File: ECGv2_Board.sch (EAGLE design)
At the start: 37 parts, among them IC1 LF347D, IC2 LF347D, IC3 TINY15LS, Q1 BS250

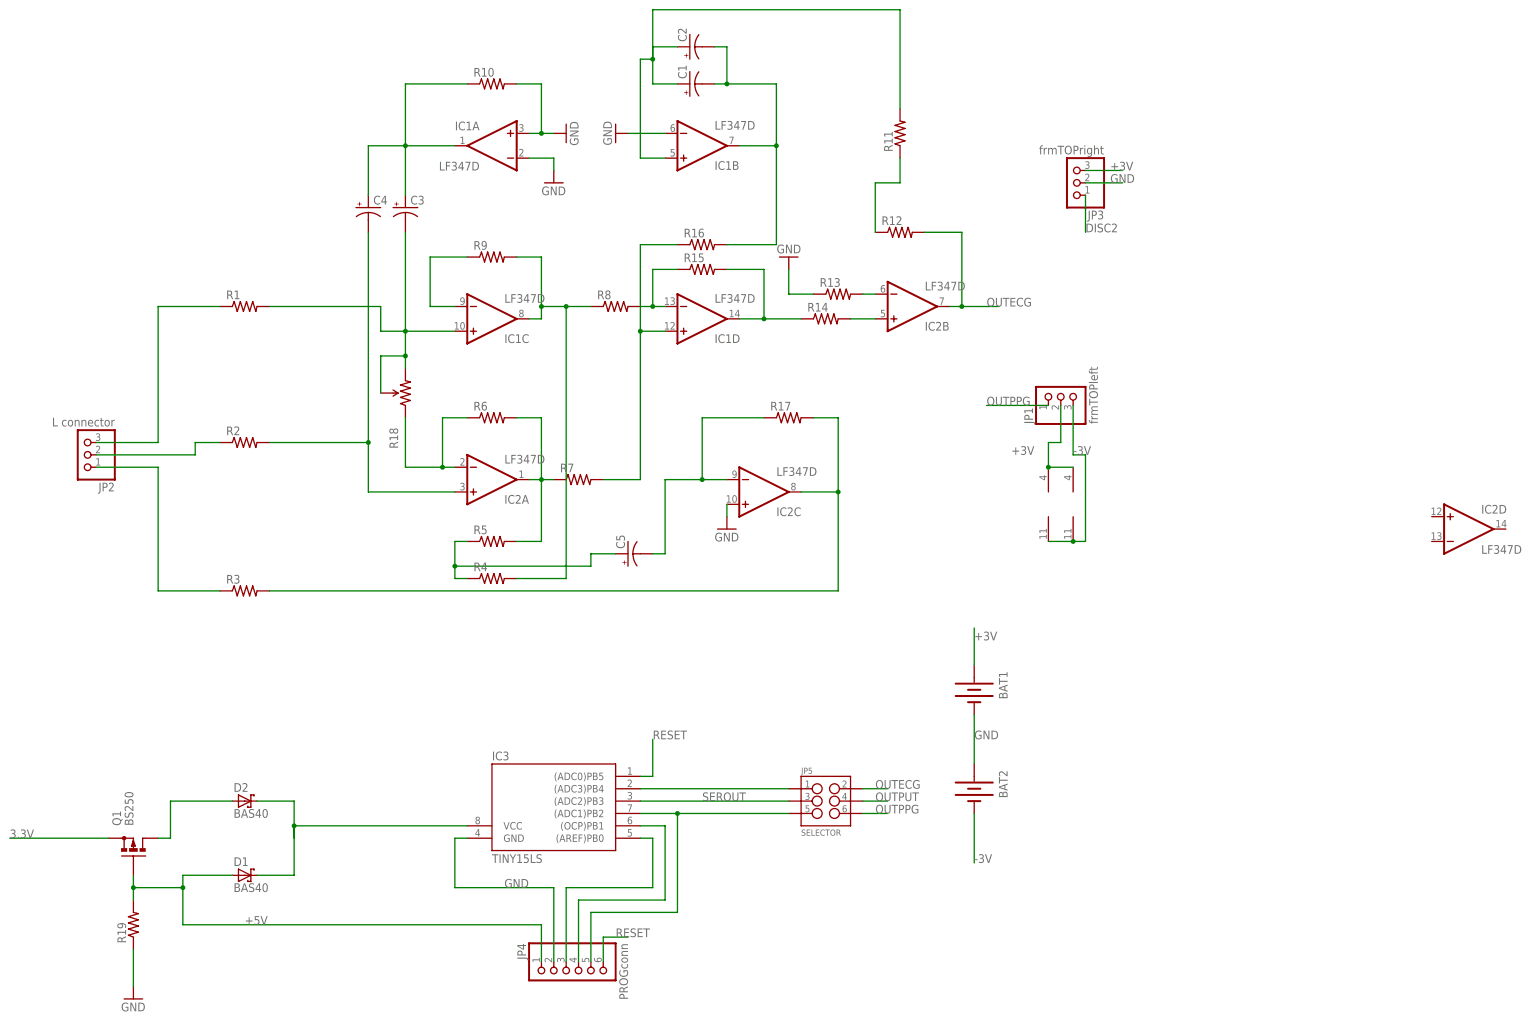
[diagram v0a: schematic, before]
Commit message: -added missing connection
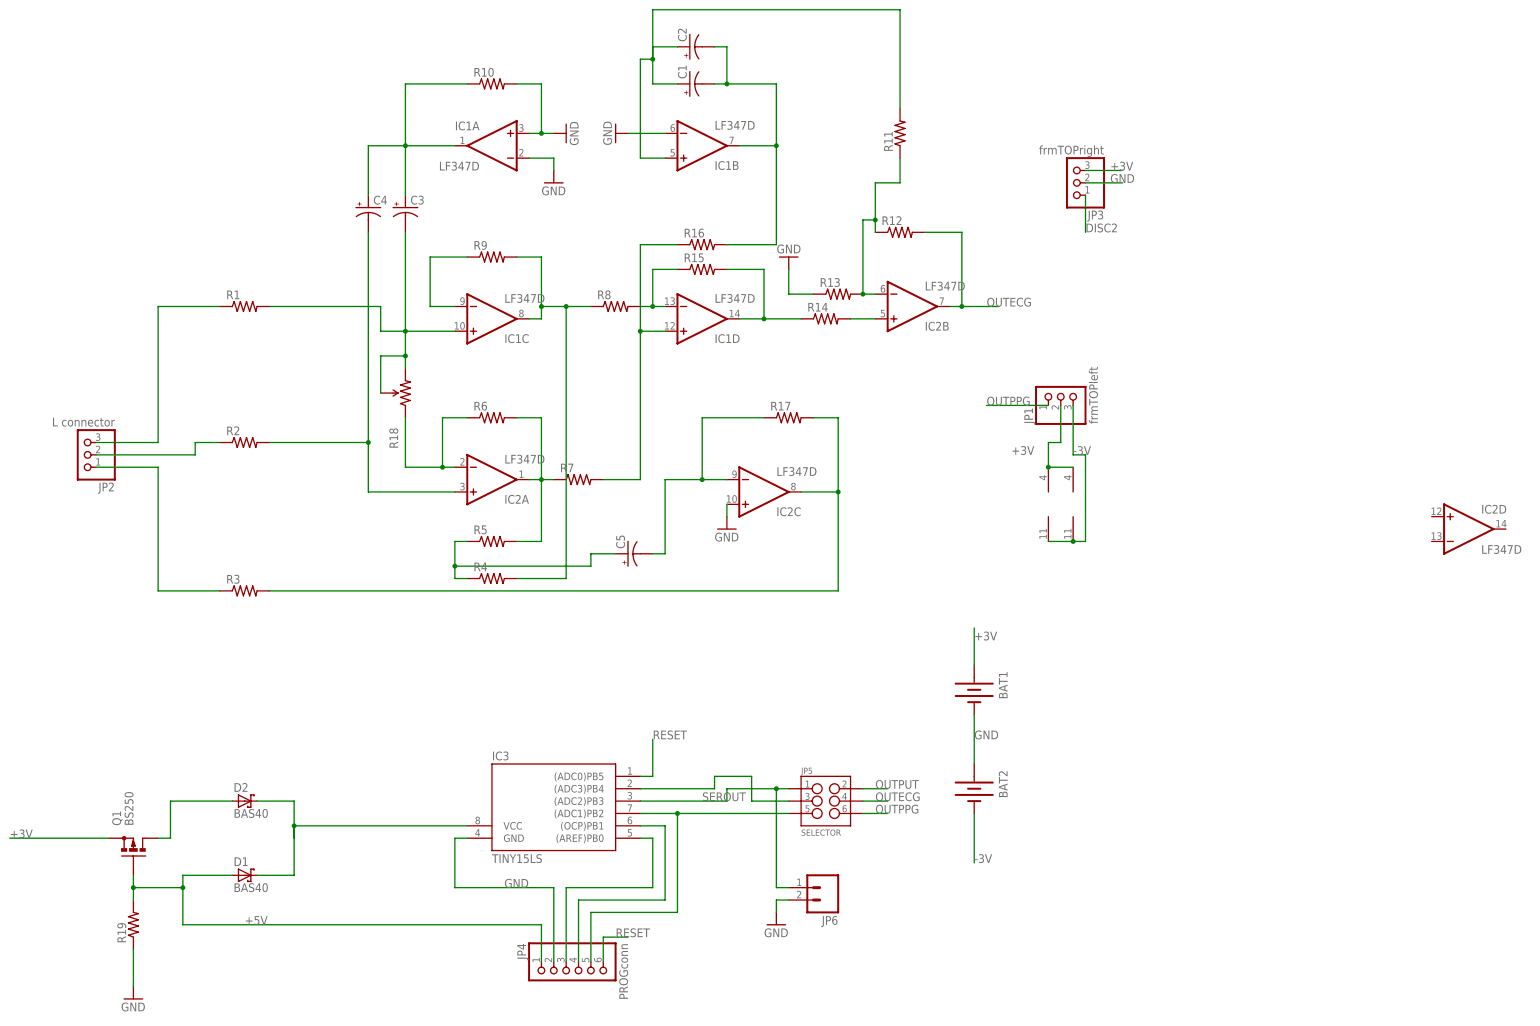
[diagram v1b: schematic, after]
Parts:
- added JP6: (no value), SparkFun-Connectors:M02PTH
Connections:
- removed net 3.3V: Q1.S
- removed net N$27: IC3.(ADC3)PB4, JP5.1
- removed net N$3: R11.1, R12.1
- new net N$28: IC3.(ADC3)PB4, JP5.3
- net +3V: now also Q1.S
- net GND: now also JP6.2
- net N$5: now also R11.1, R12.1
- net OUTECG: now also JP5.4; no longer JP5.2
- net OUTPUT: now also JP5.2; no longer JP5.4
- net SEROUT: now also JP5.1, JP6.1; no longer JP5.3
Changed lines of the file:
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@@
 <part name="GND6" library="supply1" deviceset="GND" device=""/>
 <part name="JP5" library="SparkFun-Connectors" deviceset="M03X2" device="FEMALE" value="SELECTOR"/>
+<part name="JP6" library="SparkFun-Connectors" deviceset="M02" device="PTH"/>
+<part name="GND7" library="supply1" deviceset="GND" device=""/>
 </parts>
 <sheets>
@@
 <instance part="GND6" gate="1" x="-58.42" y="-104.14"/>
 <instance part="JP5" gate="G$1" x="83.82" y="-63.5"/>
+<instance part="JP6" gate="G$1" x="83.82" y="-81.28" rot="R180"/>
+<instance part="GND7" gate="1" x="73.66" y="-88.9"/>
 </instances>
 <busses>
@@
 <wire x1="-58.42" y1="-101.6" x2="-58.42" y2="-93.98" width="0.1524" layer="91"/>
 </segment>
-</net>
-<net name="N$3" class="0">
-<segment>
-<pinref part="R11" gate="G$1" pin="1"/>
-<wire x1="99.06" y1="68.58" x2="99.06" y2="63.5" width="0.1524" layer="91"/>
-<pinref part="R12" gate="G$1" pin="1"/>
-<wire x1="99.06" y1="63.5" x2="93.98" y2="63.5" width="0.1524" layer="91"/>
-<wire x1="93.98" y1="63.5" x2="93.98" y2="53.34" width="0.1524" layer="91"/>
+<segment>
+<pinref part="JP6" gate="G$1" pin="2"/>
+<pinref part="GND7" gate="1" pin="GND"/>
+<wire x1="76.2" y1="-83.82" x2="73.66" y2="-83.82" width="0.1524" layer="91"/>
+<wire x1="73.66" y1="-83.82" x2="73.66" y2="-86.36" width="0.1524" layer="91"/>
 </segment>
 </net>
@@
 </segment>
 <segment>
-<pinref part="JP5" gate="G$1" pin="2"/>
-<wire x1="91.44" y1="-60.96" x2="96.52" y2="-60.96" width="0.1524" layer="91"/>
-<label x="93.98" y="-60.96" size="1.778" layer="95"/>
+<pinref part="JP5" gate="G$1" pin="4"/>
+<wire x1="91.44" y1="-63.5" x2="96.52" y2="-63.5" width="0.1524" layer="91"/>
+<label x="93.98" y="-63.5" size="1.778" layer="95"/>
 </segment>
 </net>
@@
 <pinref part="IC2" gate="B" pin="-IN"/>
 <wire x1="91.44" y1="40.64" x2="93.98" y2="40.64" width="0.1524" layer="91"/>
+<wire x1="91.44" y1="40.64" x2="91.44" y2="55.88" width="0.1524" layer="91"/>
+<junction x="91.44" y="40.64"/>
+<pinref part="R11" gate="G$1" pin="1"/>
+<wire x1="99.06" y1="68.58" x2="99.06" y2="63.5" width="0.1524" layer="91"/>
+<pinref part="R12" gate="G$1" pin="1"/>
+<wire x1="99.06" y1="63.5" x2="93.98" y2="63.5" width="0.1524" layer="91"/>
+<wire x1="93.98" y1="63.5" x2="93.98" y2="55.88" width="0.1524" layer="91"/>
+<wire x1="93.98" y1="55.88" x2="93.98" y2="53.34" width="0.1524" layer="91"/>
+<wire x1="91.44" y1="55.88" x2="93.98" y2="55.88" width="0.1524" layer="91"/>
+<junction x="93.98" y="55.88"/>
 </segment>
 </net>
@@
 <wire x1="114.3" y1="-35.56" x2="114.3" y2="-27.94" width="0.1524" layer="91"/>
 <label x="114.3" y="-30.48" size="1.778" layer="95"/>
+</segment>
+<segment>
+<pinref part="Q1" gate="1" pin="S"/>
+<wire x1="-63.5" y1="-71.12" x2="-83.82" y2="-71.12" width="0.1524" layer="91"/>
+<label x="-83.82" y="-71.12" size="1.778" layer="95"/>
 </segment>
 </net>
@@
 <net name="SEROUT" class="0">
 <segment>
+<label x="58.42" y="-63.5" size="1.778" layer="95"/>
+<pinref part="JP6" gate="G$1" pin="1"/>
+<wire x1="73.66" y1="-81.28" x2="76.2" y2="-81.28" width="0.1524" layer="91"/>
 <pinref part="IC3" gate="G$1" pin="(ADC2)PB3"/>
-<label x="58.42" y="-63.5" size="1.778" layer="95"/>
-<pinref part="JP5" gate="G$1" pin="3"/>
-<wire x1="45.72" y1="-63.5" x2="76.2" y2="-63.5" width="0.1524" layer="91"/>
+<wire x1="45.72" y1="-63.5" x2="63.5" y2="-63.5" width="0.1524" layer="91"/>
+<wire x1="63.5" y1="-63.5" x2="63.5" y2="-60.96" width="0.1524" layer="91"/>
+<pinref part="JP5" gate="G$1" pin="1"/>
+<wire x1="63.5" y1="-60.96" x2="73.66" y2="-60.96" width="0.1524" layer="91"/>
+<wire x1="73.66" y1="-60.96" x2="76.2" y2="-60.96" width="0.1524" layer="91"/>
+<wire x1="73.66" y1="-81.28" x2="73.66" y2="-60.96" width="0.1524" layer="91"/>
+<junction x="73.66" y="-60.96"/>
 </segment>
 </net>
@@
 </segment>
 </net>
-<net name="3.3V" class="0">
-<segment>
-<pinref part="Q1" gate="1" pin="S"/>
-<wire x1="-63.5" y1="-71.12" x2="-83.82" y2="-71.12" width="0.1524" layer="91"/>
-<label x="-83.82" y="-71.12" size="1.778" layer="95"/>
-</segment>
-</net>
 <net name="N$25" class="0">
 <segment>
@@
 </segment>
 </net>
+<net name="N$28" class="0">
+<segment>
+<pinref part="IC3" gate="G$1" pin="(ADC3)PB4"/>
+<wire x1="45.72" y1="-60.96" x2="60.96" y2="-60.96" width="0.1524" layer="91"/>
+<wire x1="60.96" y1="-60.96" x2="60.96" y2="-58.42" width="0.1524" layer="91"/>
+<wire x1="60.96" y1="-58.42" x2="68.58" y2="-58.42" width="0.1524" layer="91"/>
+<wire x1="68.58" y1="-58.42" x2="68.58" y2="-63.5" width="0.1524" layer="91"/>
+<pinref part="JP5" gate="G$1" pin="3"/>
+<wire x1="68.58" y1="-63.5" x2="76.2" y2="-63.5" width="0.1524" layer="91"/>
+</segment>
+</net>
 <net name="OUTPUT" class="0">
 <segment>
-<pinref part="JP5" gate="G$1" pin="4"/>
-<wire x1="91.44" y1="-63.5" x2="96.52" y2="-63.5" width="0.1524" layer="91"/>
-<label x="93.98" y="-63.5" size="1.778" layer="95"/>
-</segment>
-</net>
-<net name="N$27" class="0">
-<segment>
-<pinref part="IC3" gate="G$1" pin="(ADC3)PB4"/>
-<pinref part="JP5" gate="G$1" pin="1"/>
-<wire x1="45.72" y1="-60.96" x2="76.2" y2="-60.96" width="0.1524" layer="91"/>
-</segment>
-</net>
+<pinref part="JP5" gate="G$1" pin="2"/>
+<wire x1="91.44" y1="-60.96" x2="96.52" y2="-60.96" width="0.1524" layer="91"/>
+<label x="93.98" y="-60.96" size="1.778" layer="95"/>
+</segment>
+</net>

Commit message: Major changes
-final commit
-some corrections
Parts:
- Q1: value BS250 -> BSS84; device transistor-small-signal:BS250 -> transistor-small-signal:BSS84
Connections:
- removed net N$11: IC1C.-IN, R9.1
- new net N$3: IC1C.-IN, R18.CW, R18.WIPER, R9.1
- net GND: now also IC1B.+IN; no longer IC1B.-IN
- net N$19: no longer R18.CW, R18.WIPER
- net N$2: now also IC1B.-IN; no longer IC1B.+IN
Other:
- moved on the sheet: R7, R8
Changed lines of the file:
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@@
 <part name="BAT1" library="SparkFun-Electromechanical" deviceset="BATTERY" device="245MM"/>
 <part name="BAT2" library="SparkFun-Electromechanical" deviceset="BATTERY" device="245MM"/>
-<part name="Q1" library="transistor-small-signal" deviceset="BS250" device=""/>
+<part name="Q1" library="transistor-small-signal" deviceset="BSS84" device=""/>
 <part name="R19" library="SparkFun-Passives" deviceset="RESISTOR" device="0402-RES"/>
 <part name="GND6" library="supply1" deviceset="GND" device=""/>
@@
 <instance part="GND1" gate="1" x="27.94" y="63.5"/>
 <instance part="GND2" gate="1" x="30.48" y="73.66" rot="R90"/>
-<instance part="GND3" gate="1" x="40.64" y="73.66" rot="R270"/>
+<instance part="GND3" gate="1" x="40.64" y="68.58" rot="R270"/>
 <instance part="GND4" gate="1" x="63.5" y="-7.62"/>
 <instance part="GND5" gate="1" x="76.2" y="48.26" rot="R180"/>
@@
 <instance part="R5" gate="G$1" x="15.24" y="-10.16"/>
 <instance part="R6" gate="G$1" x="15.24" y="15.24"/>
-<instance part="R7" gate="G$1" x="33.02" y="2.54"/>
-<instance part="R8" gate="G$1" x="40.64" y="38.1"/>
+<instance part="R7" gate="G$1" x="38.1" y="2.54"/>
+<instance part="R8" gate="G$1" x="38.1" y="38.1"/>
 <instance part="R9" gate="G$1" x="15.24" y="48.26"/>
 <instance part="R10" gate="G$1" x="15.24" y="83.82"/>
@@
 <instance part="BAT1" gate="G$1" x="114.3" y="-40.64" rot="R270"/>
 <instance part="BAT2" gate="G$1" x="114.3" y="-60.96" rot="R270"/>
-<instance part="Q1" gate="1" x="-58.42" y="-73.66" rot="R90"/>
+<instance part="Q1" gate="G$1" x="-60.96" y="-71.12" rot="R90"/>
 <instance part="R19" gate="G$1" x="-58.42" y="-88.9" rot="R90"/>
 <instance part="GND6" gate="1" x="-58.42" y="-104.14"/>
@@
 <wire x1="48.26" y1="91.44" x2="53.34" y2="91.44" width="0.1524" layer="91"/>
 <wire x1="48.26" y1="88.9" x2="45.72" y2="88.9" width="0.1524" layer="91"/>
-<wire x1="45.72" y1="88.9" x2="45.72" y2="68.58" width="0.1524" layer="91"/>
 <junction x="48.26" y="88.9"/>
 <wire x1="48.26" y1="88.9" x2="48.26" y2="99.06" width="0.1524" layer="91"/>
@@
 <wire x1="48.26" y1="99.06" x2="99.06" y2="99.06" width="0.1524" layer="91"/>
 <wire x1="99.06" y1="99.06" x2="99.06" y2="78.74" width="0.1524" layer="91"/>
-<pinref part="IC1" gate="B" pin="+IN"/>
-<wire x1="45.72" y1="68.58" x2="50.8" y2="68.58" width="0.1524" layer="91"/>
+<wire x1="45.72" y1="88.9" x2="45.72" y2="73.66" width="0.1524" layer="91"/>
+<pinref part="IC1" gate="B" pin="-IN"/>
+<wire x1="45.72" y1="73.66" x2="50.8" y2="73.66" width="0.1524" layer="91"/>
 </segment>
 </net>
@@
 </segment>
 <segment>
-<pinref part="GND3" gate="1" pin="GND"/>
-<pinref part="IC1" gate="B" pin="-IN"/>
-<wire x1="43.18" y1="73.66" x2="50.8" y2="73.66" width="0.1524" layer="91"/>
-</segment>
-<segment>
 <pinref part="GND4" gate="1" pin="GND"/>
 <pinref part="IC2" gate="C" pin="+IN"/>
@@
 <wire x1="76.2" y1="-83.82" x2="73.66" y2="-83.82" width="0.1524" layer="91"/>
 <wire x1="73.66" y1="-83.82" x2="73.66" y2="-86.36" width="0.1524" layer="91"/>
+</segment>
+<segment>
+<pinref part="GND3" gate="1" pin="GND"/>
+<pinref part="IC1" gate="B" pin="+IN"/>
+<wire x1="43.18" y1="68.58" x2="50.8" y2="68.58" width="0.1524" layer="91"/>
 </segment>
 </net>
@@
 <wire x1="48.26" y1="45.72" x2="48.26" y2="38.1" width="0.1524" layer="91"/>
 <pinref part="R8" gate="G$1" pin="2"/>
-<wire x1="48.26" y1="38.1" x2="45.72" y2="38.1" width="0.1524" layer="91"/>
+<wire x1="48.26" y1="38.1" x2="43.18" y2="38.1" width="0.1524" layer="91"/>
 <pinref part="IC1" gate="D" pin="-IN"/>
 <wire x1="50.8" y1="38.1" x2="48.26" y2="38.1" width="0.1524" layer="91"/>
@@
 <wire x1="53.34" y1="50.8" x2="45.72" y2="50.8" width="0.1524" layer="91"/>
 <pinref part="R7" gate="G$1" pin="2"/>
-<wire x1="38.1" y1="2.54" x2="45.72" y2="2.54" width="0.1524" layer="91"/>
+<wire x1="43.18" y1="2.54" x2="45.72" y2="2.54" width="0.1524" layer="91"/>
 <wire x1="45.72" y1="2.54" x2="45.72" y2="33.02" width="0.1524" layer="91"/>
 <pinref part="IC1" gate="D" pin="+IN"/>
@@
 <wire x1="22.86" y1="2.54" x2="25.4" y2="2.54" width="0.1524" layer="91"/>
 <pinref part="R6" gate="G$1" pin="2"/>
-<wire x1="25.4" y1="2.54" x2="27.94" y2="2.54" width="0.1524" layer="91"/>
+<wire x1="25.4" y1="2.54" x2="33.02" y2="2.54" width="0.1524" layer="91"/>
 <wire x1="20.32" y1="15.24" x2="25.4" y2="15.24" width="0.1524" layer="91"/>
 <wire x1="25.4" y1="15.24" x2="25.4" y2="2.54" width="0.1524" layer="91"/>
@@
 <segment>
 <pinref part="R8" gate="G$1" pin="1"/>
-<wire x1="35.56" y1="38.1" x2="30.48" y2="38.1" width="0.1524" layer="91"/>
+<wire x1="33.02" y1="38.1" x2="30.48" y2="38.1" width="0.1524" layer="91"/>
 <wire x1="30.48" y1="38.1" x2="25.4" y2="38.1" width="0.1524" layer="91"/>
 <wire x1="25.4" y1="38.1" x2="25.4" y2="35.56" width="0.1524" layer="91"/>
@@
 </segment>
 </net>
-<net name="N$11" class="0">
-<segment>
-<pinref part="R9" gate="G$1" pin="1"/>
-<wire x1="10.16" y1="48.26" x2="2.54" y2="48.26" width="0.1524" layer="91"/>
-<wire x1="2.54" y1="48.26" x2="2.54" y2="38.1" width="0.1524" layer="91"/>
-<pinref part="IC1" gate="C" pin="-IN"/>
-<wire x1="2.54" y1="38.1" x2="7.62" y2="38.1" width="0.1524" layer="91"/>
-</segment>
-</net>
 <net name="N$12" class="0">
 <segment>
@@
 <net name="N$19" class="0">
 <segment>
-<pinref part="R18" gate="R?" pin="WIPER"/>
-<wire x1="-7.62" y1="20.32" x2="-7.62" y2="27.94" width="0.1524" layer="91"/>
-<pinref part="R18" gate="R?" pin="CW"/>
-<wire x1="-7.62" y1="27.94" x2="-2.54" y2="27.94" width="0.1524" layer="91"/>
-<wire x1="-2.54" y1="27.94" x2="-2.54" y2="25.4" width="0.1524" layer="91"/>
-<pinref part="C3" gate="G$1" pin="-"/>
-<wire x1="-2.54" y1="53.34" x2="-2.54" y2="33.02" width="0.1524" layer="91"/>
 <pinref part="R1" gate="G$1" pin="2"/>
 <wire x1="-30.48" y1="38.1" x2="-7.62" y2="38.1" width="0.1524" layer="91"/>
 <wire x1="-7.62" y1="38.1" x2="-7.62" y2="33.02" width="0.1524" layer="91"/>
+<pinref part="IC1" gate="C" pin="+IN"/>
 <wire x1="-7.62" y1="33.02" x2="-2.54" y2="33.02" width="0.1524" layer="91"/>
+<pinref part="C3" gate="G$1" pin="-"/>
+<wire x1="-2.54" y1="33.02" x2="7.62" y2="33.02" width="0.1524" layer="91"/>
+<wire x1="-2.54" y1="53.34" x2="-2.54" y2="33.02" width="0.1524" layer="91"/>
 <junction x="-2.54" y="33.02"/>
-<wire x1="-2.54" y1="27.94" x2="-2.54" y2="33.02" width="0.1524" layer="91"/>
-<junction x="-2.54" y="27.94"/>
-<pinref part="IC1" gate="C" pin="+IN"/>
-<wire x1="-2.54" y1="33.02" x2="7.62" y2="33.02" width="0.1524" layer="91"/>
 </segment>
 </net>
@@
 </segment>
 <segment>
-<pinref part="Q1" gate="1" pin="S"/>
-<wire x1="-63.5" y1="-71.12" x2="-83.82" y2="-71.12" width="0.1524" layer="91"/>
+<pinref part="Q1" gate="G$1" pin="S"/>
+<wire x1="-66.04" y1="-71.12" x2="-83.82" y2="-71.12" width="0.1524" layer="91"/>
 <label x="-83.82" y="-71.12" size="1.778" layer="95"/>
 </segment>
@@
 <wire x1="-48.26" y1="-88.9" x2="-48.26" y2="-81.28" width="0.1524" layer="91"/>
 <pinref part="R19" gate="G$1" pin="2"/>
-<pinref part="Q1" gate="1" pin="G"/>
+<pinref part="Q1" gate="G$1" pin="G"/>
 <wire x1="-58.42" y1="-83.82" x2="-58.42" y2="-81.28" width="0.1524" layer="91"/>
-<wire x1="-58.42" y1="-81.28" x2="-58.42" y2="-78.74" width="0.1524" layer="91"/>
+<wire x1="-58.42" y1="-81.28" x2="-63.5" y2="-76.2" width="0.1524" layer="91"/>
 <wire x1="-48.26" y1="-81.28" x2="-58.42" y2="-81.28" width="0.1524" layer="91"/>
 <junction x="-58.42" y="-81.28"/>
@@
 <wire x1="-38.1" y1="-63.5" x2="-50.8" y2="-63.5" width="0.1524" layer="91"/>
 <wire x1="-50.8" y1="-63.5" x2="-50.8" y2="-71.12" width="0.1524" layer="91"/>
-<pinref part="Q1" gate="1" pin="D"/>
-<wire x1="-50.8" y1="-71.12" x2="-53.34" y2="-71.12" width="0.1524" layer="91"/>
+<pinref part="Q1" gate="G$1" pin="D"/>
+<wire x1="-50.8" y1="-71.12" x2="-55.88" y2="-71.12" width="0.1524" layer="91"/>
 </segment>
 </net>
@@
 </segment>
 </net>
+<net name="N$3" class="0">
+<segment>
+<pinref part="R18" gate="R?" pin="CW"/>
+<wire x1="-2.54" y1="27.94" x2="-2.54" y2="25.4" width="0.1524" layer="91"/>
+<wire x1="-7.62" y1="27.94" x2="-2.54" y2="27.94" width="0.1524" layer="91"/>
+<pinref part="R18" gate="R?" pin="WIPER"/>
+<wire x1="-7.62" y1="20.32" x2="-7.62" y2="27.94" width="0.1524" layer="91"/>
+<pinref part="R9" gate="G$1" pin="1"/>
+<wire x1="10.16" y1="48.26" x2="2.54" y2="48.26" width="0.1524" layer="91"/>
+<wire x1="2.54" y1="48.26" x2="2.54" y2="38.1" width="0.1524" layer="91"/>
+<pinref part="IC1" gate="C" pin="-IN"/>
+<wire x1="2.54" y1="38.1" x2="7.62" y2="38.1" width="0.1524" layer="91"/>
+<wire x1="-2.54" y1="27.94" x2="2.54" y2="27.94" width="0.1524" layer="91"/>
+<wire x1="2.54" y1="27.94" x2="2.54" y2="38.1" width="0.1524" layer="91"/>
+<junction x="-2.54" y="27.94"/>
+<junction x="2.54" y="38.1"/>
+</segment>
+</net>
